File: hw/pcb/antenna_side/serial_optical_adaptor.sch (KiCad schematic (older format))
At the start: 28 parts, among them IC1 ATMEGA168PA-A, P1 CONN_02X03, P2 Battery, P3 CONN_01X01, P4 CONN_01X04, U1 LM393, U2 LP3984, U3 ADG3300

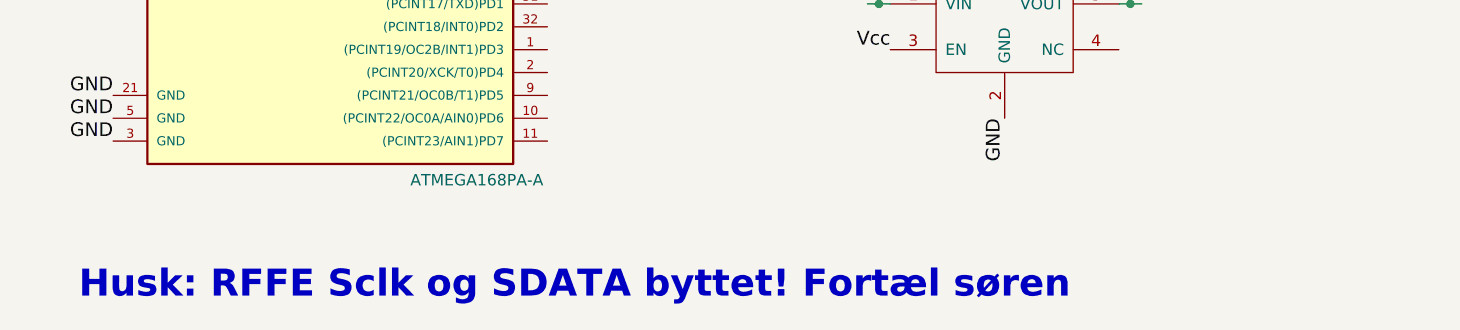
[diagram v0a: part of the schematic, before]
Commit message: 
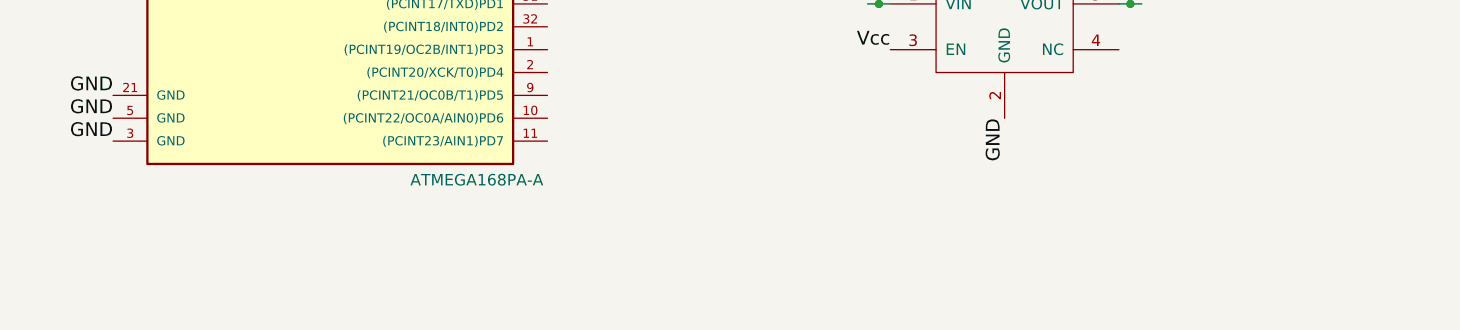
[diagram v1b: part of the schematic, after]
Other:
- note removed: "Husk: RFFE Sclk og SDATA byttet! Fortæl søren\n"
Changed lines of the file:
@@
 Text Label 6850 4600 0    60   ~ 0
 GND
-Text Notes 850  7700 0    118  ~ 24
-Husk: RFFE Sclk og SDATA byttet! Fortæl søren\n
 $EndSCHEMATC

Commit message: 123
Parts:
- R10, R11: value R -> 0
- R8, R9: value R -> 10k
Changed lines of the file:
@@
 P 5800 4900
 F 0 "R8" V 5880 4900 50  0000 C CNN
-F 1 "R" V 5800 4900 50  0000 C CNN
+F 1 "10k" V 5800 4900 50  0000 C CNN
 F 2 "Resistors_SMD:R_0603_HandSoldering" V 5730 4900 50  0001 C CNN
 F 3 "" H 5800 4900 50  0000 C CNN
@@
 P 5800 5300
 F 0 "R9" V 5880 5300 50  0000 C CNN
-F 1 "R" V 5800 5300 50  0000 C CNN
+F 1 "10k" V 5800 5300 50  0000 C CNN
 F 2 "Resistors_SMD:R_0603_HandSoldering" V 5730 5300 50  0001 C CNN
 F 3 "" H 5800 5300 50  0000 C CNN
@@
 P 6850 4450
 F 0 "R10" V 6930 4450 50  0000 C CNN
-F 1 "R" V 6850 4450 50  0000 C CNN
+F 1 "0" V 6850 4450 50  0000 C CNN
 F 2 "Resistors_SMD:R_0603_HandSoldering" V 6780 4450 50  0001 C CNN
 F 3 "" H 6850 4450 50  0000 C CNN
@@
 P 7050 4450
 F 0 "R11" V 7130 4450 50  0000 C CNN
-F 1 "R" V 7050 4450 50  0000 C CNN
+F 1 "0" V 7050 4450 50  0000 C CNN
 F 2 "Resistors_SMD:R_0603_HandSoldering" V 6980 4450 50  0001 C CNN
 F 3 "" H 7050 4450 50  0000 C CNN

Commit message: Updated values
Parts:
- added R12: 0, Resistors_SMD:R_0603_HandSoldering, symbol R
- C1, C2, C3, C4, C5, C6: value C -> 100n
- P2: footprint hw:SMTU2032-1 -> antenna_side:Batt
- R8, R9: value 10k -> 100k
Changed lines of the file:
@@
 P 5450 6250
 F 0 "C6" H 5475 6350 50  0000 L CNN
-F 1 "C" H 5350 6350 50  0000 L CNN
+F 1 "100n" H 5350 6350 50  0000 R CNN
 F 2 "Capacitors_SMD:C_0603_HandSoldering" H 5488 6100 50  0001 C CNN
 F 3 "" H 5450 6250 50  0000 C CNN
@@
 P 4350 6250
 F 0 "C5" H 4375 6350 50  0000 L CNN
-F 1 "C" H 4375 6150 50  0000 L CNN
+F 1 "100n" H 4375 6150 50  0000 L CNN
 F 2 "Capacitors_SMD:C_0603_HandSoldering" H 4388 6100 50  0001 C CNN
 F 3 "" H 4350 6250 50  0000 C CNN
@@
 P 950 4150
 F 0 "C1" H 975 4250 50  0000 L CNN
-F 1 "C" H 975 4050 50  0000 L CNN
+F 1 "100n" H 975 4050 50  0000 L CNN
 F 2 "Capacitors_SMD:C_0603_HandSoldering" H 988 4000 50  0001 C CNN
 F 3 "" H 950 4150 50  0000 C CNN
@@
 P 1200 4150
 F 0 "C2" H 1225 4250 50  0000 L CNN
-F 1 "C" H 1225 4050 50  0000 L CNN
+F 1 "100n" H 1225 4050 50  0000 L CNN
 F 2 "Capacitors_SMD:C_0603_HandSoldering" H 1238 4000 50  0001 C CNN
 F 3 "" H 1200 4150 50  0000 C CNN
@@
 P 1450 4150
 F 0 "C3" H 1475 4250 50  0000 L CNN
-F 1 "C" H 1475 4050 50  0000 L CNN
+F 1 "100n" H 1475 4050 50  0000 L CNN
 F 2 "Capacitors_SMD:C_0603_HandSoldering" H 1488 4000 50  0001 C CNN
 F 3 "" H 1450 4150 50  0000 C CNN
@@
 P 1700 4150
 F 0 "C4" H 1725 4250 50  0000 L CNN
-F 1 "C" H 1725 4050 50  0000 L CNN
+F 1 "100n" H 1725 4050 50  0000 L CNN
 F 2 "Capacitors_SMD:C_0603_HandSoldering" H 1738 4000 50  0001 C CNN
 F 3 "" H 1700 4150 50  0000 C CNN
@@
 P 5800 4900
 F 0 "R8" V 5880 4900 50  0000 C CNN
-F 1 "10k" V 5800 4900 50  0000 C CNN
+F 1 "100k" V 5800 4900 50  0000 C CNN
 F 2 "Resistors_SMD:R_0603_HandSoldering" V 5730 4900 50  0001 C CNN
 F 3 "" H 5800 4900 50  0000 C CNN
@@
 P 5800 5300
 F 0 "R9" V 5880 5300 50  0000 C CNN
-F 1 "10k" V 5800 5300 50  0000 C CNN
+F 1 "100k" V 5800 5300 50  0000 C CNN
 F 2 "Resistors_SMD:R_0603_HandSoldering" V 5730 5300 50  0001 C CNN
 F 3 "" H 5800 5300 50  0000 C CNN
@@
 F 0 "P2" H 4450 4200 50  0000 C CNN
 F 1 "Battery" V 4550 4050 50  0000 C CNN
-F 2 "hw:SMTU2032-1" H 4450 4050 50  0001 C CNN
+F 2 "antenna_side:Batt" H 4450 4050 50  0001 C CNN
 F 3 "" H 4450 4050 50  0000 C CNN
 	1    4450 4050
@@
 Text Label 6850 4600 0    60   ~ 0
 GND
+$Comp
+L R R12
+U 1 1 57065C86
+P 7400 4450
+F 0 "R12" V 7480 4450 50  0000 C CNN
+F 1 "0" V 7400 4450 50  0000 C CNN
+F 2 "Resistors_SMD:R_0603_HandSoldering" V 7330 4450 50  0001 C CNN
+F 3 "" H 7400 4450 50  0000 C CNN
+	1    7400 4450
+	1    0    0    -1
+$EndComp
+Text Label 7400 4300 0    60   ~ 0
+GND
+Text Label 7400 4600 0    60   ~ 0
+GND
 $EndSCHEMATC
